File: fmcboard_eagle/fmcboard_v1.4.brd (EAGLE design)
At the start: 147 x 74 mm, 160 parts, among them IC1 OPA699ID, IC10 LTC6229IMS8E#TRPBF, IC11 7805TV, IC12 SN74AUC2G66DCTR, IC13 SN74AUC2G66DCTR, IC14 SN74AUC2G66DCTR, IC15 SN74AUC2G66DCTR, IC16 DAC7578SPWR, IC2 DAC7578SPWR, IC3 LTC6229IMS8E#TRPBF, IC4 LTC6229IMS8E#TRPBF, IC5 LM358, IC6 OPA699ID, IC7 OPA699ID, IC8 LTC6229IMS8E#TRPBF, IC9 LTC6229IMS8E#TRPBF, J1 8pin, J10 8pin, J12 4p-2.54, J2 ASP-134604-01, J3 4p-2.54, J4 4p-2.54, J5 8pin, J6 4p-2.54, J7 4p-2.54, J8 4p-2.54, J9 8pin, U1 TXS0108EPWR, U2 STMICROELECTRONICS_L7905ACVST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

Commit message: v1.43 ordered
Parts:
- R11: value 5k -> 4.7k
- R14, R25, R31: value 4k -> 4.7k
- R2, R34: value 50 -> 47
- R35: value 4k -> 4.7K
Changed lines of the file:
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@@
 <attribute name="VALUE" x="79.635" y="45.54" size="0.8128" layer="21" rot="R180"/>
 </element>
-<element name="R14" library="rcl" library_urn="urn:adsk.eagle:library:334" package="R0805" package3d_urn="urn:adsk.eagle:package:23553/2" value="4k" x="76" y="45" smashed="yes" rot="R180">
+<element name="R14" library="rcl" library_urn="urn:adsk.eagle:library:334" package="R0805" package3d_urn="urn:adsk.eagle:package:23553/2" value="4.7k" x="76" y="45" smashed="yes" rot="R180">
 <attribute name="POPULARITY" value="85" x="76" y="45" size="1.778" layer="27" rot="R180" display="off"/>
 <attribute name="SPICEPREFIX" value="R" x="76" y="45" size="1.778" layer="27" rot="R180" display="off"/>
@@
 <attribute name="VALUE" x="96.365" y="27.46" size="0.8128" layer="21"/>
 </element>
-<element name="R11" library="rcl" library_urn="urn:adsk.eagle:library:334" package="R0805" package3d_urn="urn:adsk.eagle:package:23553/2" value="5k" x="82" y="48" smashed="yes">
+<element name="R11" library="rcl" library_urn="urn:adsk.eagle:library:334" package="R0805" package3d_urn="urn:adsk.eagle:package:23553/2" value="4.7k" x="82" y="48" smashed="yes">
 <attribute name="POPULARITY" value="85" x="76" y="55" size="0.8128" layer="27" display="off"/>
 <attribute name="SPICEPREFIX" value="R" x="76" y="55" size="0.8128" layer="27" display="off"/>
@@
 <attribute name="VALUE" x="79.635" y="42.54" size="0.8128" layer="21" rot="R180"/>
 </element>
-<element name="R25" library="rcl" library_urn="urn:adsk.eagle:library:334" package="R0805" package3d_urn="urn:adsk.eagle:package:23553/2" value="4k" x="76" y="42" smashed="yes" rot="R180">
+<element name="R25" library="rcl" library_urn="urn:adsk.eagle:library:334" package="R0805" package3d_urn="urn:adsk.eagle:package:23553/2" value="4.7k" x="76" y="42" smashed="yes" rot="R180">
 <attribute name="POPULARITY" value="85" x="82" y="61" size="0.8128" layer="27" rot="R180" display="off"/>
 <attribute name="SPICEPREFIX" value="R" x="82" y="61" size="0.8128" layer="27" rot="R180" display="off"/>
@@
 <attribute name="VALUE" x="96.365" y="44.46" size="0.8128" layer="21"/>
 </element>
-<element name="R2" library="rcl" library_urn="urn:adsk.eagle:library:334" package="R0805" package3d_urn="urn:adsk.eagle:package:23553/2" value="50" x="82" y="52" smashed="yes" rot="R180">
+<element name="R2" library="rcl" library_urn="urn:adsk.eagle:library:334" package="R0805" package3d_urn="urn:adsk.eagle:package:23553/2" value="47" x="82" y="52" smashed="yes" rot="R180">
 <attribute name="POPULARITY" value="85" x="82" y="52" size="1.778" layer="27" rot="R180" display="off"/>
 <attribute name="SPICEPREFIX" value="R" x="82" y="52" size="1.778" layer="27" rot="R180" display="off"/>
@@
 <attribute name="VALUE" x="80.016" y="50.397" size="0.8128" layer="21" rot="R180"/>
 </element>
-<element name="R34" library="rcl" library_urn="urn:adsk.eagle:library:334" package="R0805" package3d_urn="urn:adsk.eagle:package:23553/2" value="50" x="94" y="52" smashed="yes">
+<element name="R34" library="rcl" library_urn="urn:adsk.eagle:library:334" package="R0805" package3d_urn="urn:adsk.eagle:package:23553/2" value="47" x="94" y="52" smashed="yes">
 <attribute name="POPULARITY" value="85" x="94" y="52" size="1.778" layer="27" display="off"/>
 <attribute name="SPICEPREFIX" value="R" x="94" y="52" size="1.778" layer="27" display="off"/>
@@
 </element>
 <element name="C55" library="SparkFun-Passives" package="0805" value="0.1uF" x="114" y="49" smashed="yes"/>
-<element name="R31" library="rcl" library_urn="urn:adsk.eagle:library:334" package="R0805" package3d_urn="urn:adsk.eagle:package:23553/2" value="4k" x="114" y="37" smashed="yes">
+<element name="R31" library="rcl" library_urn="urn:adsk.eagle:library:334" package="R0805" package3d_urn="urn:adsk.eagle:package:23553/2" value="4.7k" x="114" y="37" smashed="yes">
 <attribute name="POPULARITY" value="85" x="114" y="37" size="1.778" layer="27" display="off"/>
 <attribute name="SPICEPREFIX" value="R" x="114" y="37" size="1.778" layer="27" display="off"/>
 </element>
-<element name="R35" library="rcl" library_urn="urn:adsk.eagle:library:334" package="R0805" package3d_urn="urn:adsk.eagle:package:23553/2" value="4k" x="114" y="34" smashed="yes">
+<element name="R35" library="rcl" library_urn="urn:adsk.eagle:library:334" package="R0805" package3d_urn="urn:adsk.eagle:package:23553/2" value="4.7K" x="114" y="34" smashed="yes">
 <attribute name="POPULARITY" value="85" x="114" y="34" size="1.778" layer="27" display="off"/>
 <attribute name="SPICEPREFIX" value="R" x="114" y="34" size="1.778" layer="27" display="off"/>

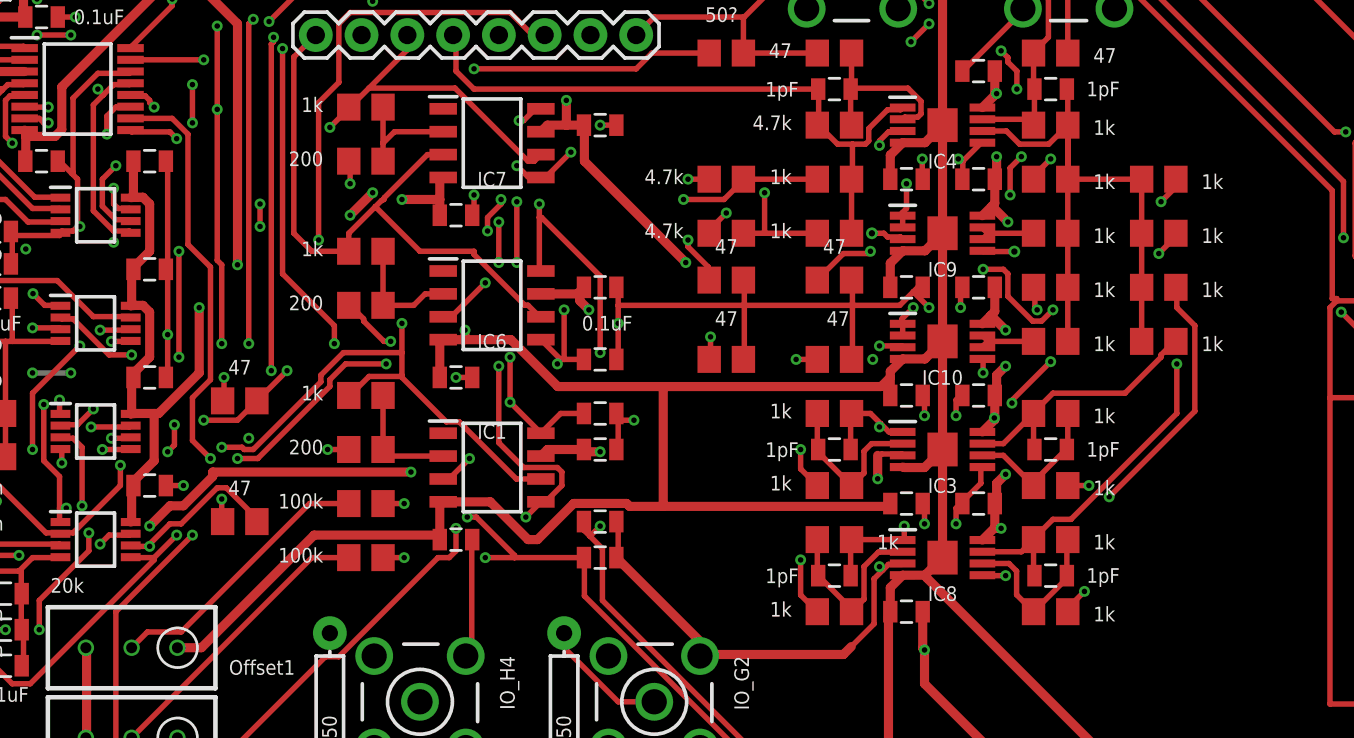
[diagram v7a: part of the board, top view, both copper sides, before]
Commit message: 100 Ohm neg pulse and neg sum feedback resistors 4.7k->1k transimpedance resistor
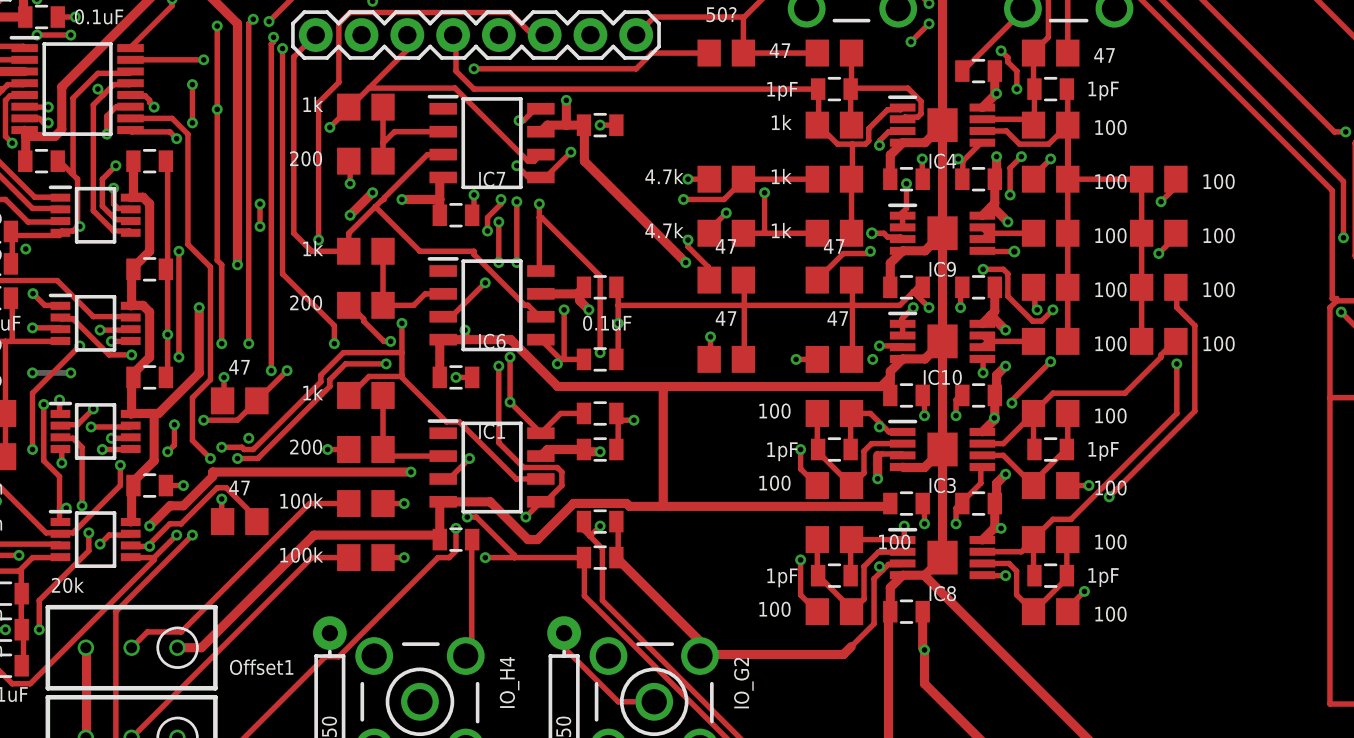
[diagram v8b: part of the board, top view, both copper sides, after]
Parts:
- R1, R12, R21, R22, R23, R24, R27, R28, R29, R30, R32, R33, R36, R38, R40, R7, R8: value 1k -> 100
- R11: value 4.7k -> 1k
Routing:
- net C10: track 101.9 -> 98.3 mm, vias 12 -> 11
